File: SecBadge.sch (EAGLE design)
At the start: 21 parts, among them J1 USB_A, U1 32U4, Y1 16MHz

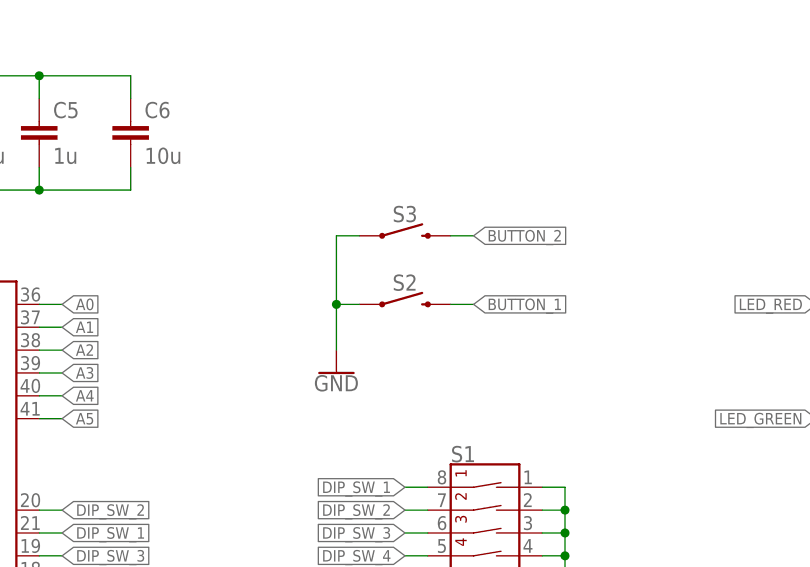
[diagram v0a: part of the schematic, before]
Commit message: Added button designator in schematic.
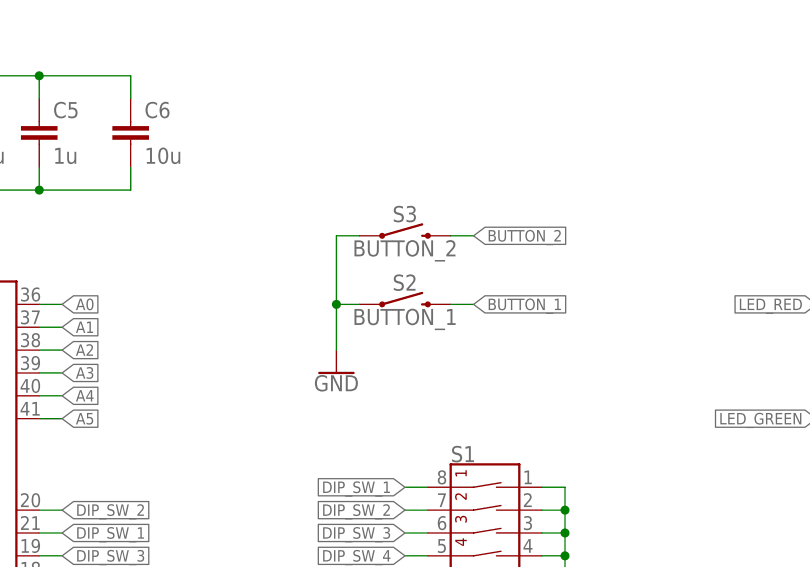
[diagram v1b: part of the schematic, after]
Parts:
- S2: value MOMENTARY-SWITCH-SPST-PTH-6.0MM -> BUTTON_1
- S3: value MOMENTARY-SWITCH-SPST-PTH-6.0MM -> BUTTON_2
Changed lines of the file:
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@@
 <part name="D1" library="ZnibbLib" deviceset="LED" device="" value="RED"/>
 <part name="D2" library="ZnibbLib" deviceset="LED" device="" value="GREEN"/>
-<part name="S2" library="SparkFun-Switches" deviceset="MOMENTARY-SWITCH-SPST" device="-PTH-6.0MM" value=""/>
-<part name="S3" library="SparkFun-Switches" deviceset="MOMENTARY-SWITCH-SPST" device="-PTH-6.0MM" value=""/>
+<part name="S2" library="SparkFun-Switches" deviceset="MOMENTARY-SWITCH-SPST" device="-PTH-6.0MM" value="BUTTON_1"/>
+<part name="S3" library="SparkFun-Switches" deviceset="MOMENTARY-SWITCH-SPST" device="-PTH-6.0MM" value="BUTTON_2"/>
 <part name="R4" library="ZnibbLib" deviceset="RESISTOR" device="1206" value="150"/>
 <part name="R5" library="ZnibbLib" deviceset="RESISTOR" device="1206" value="90"/>

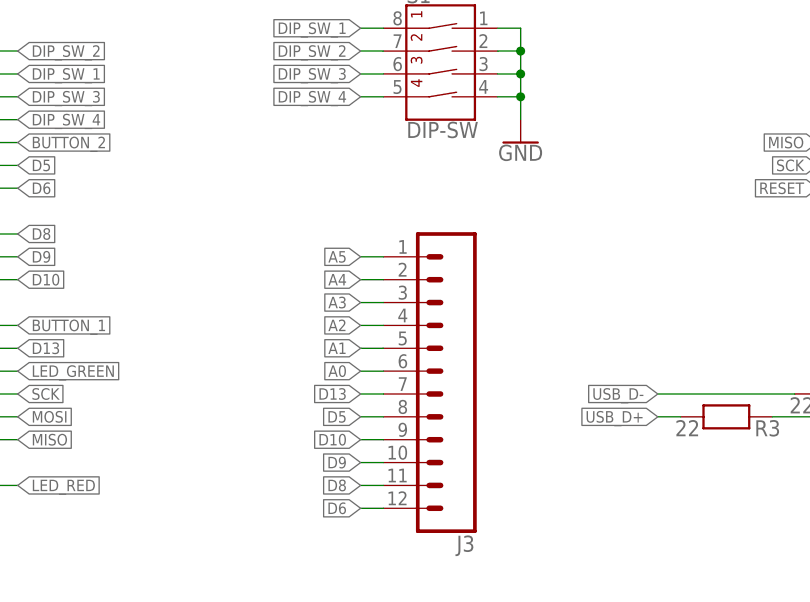
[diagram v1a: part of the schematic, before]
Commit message: Added VCC and GND to expansion header.
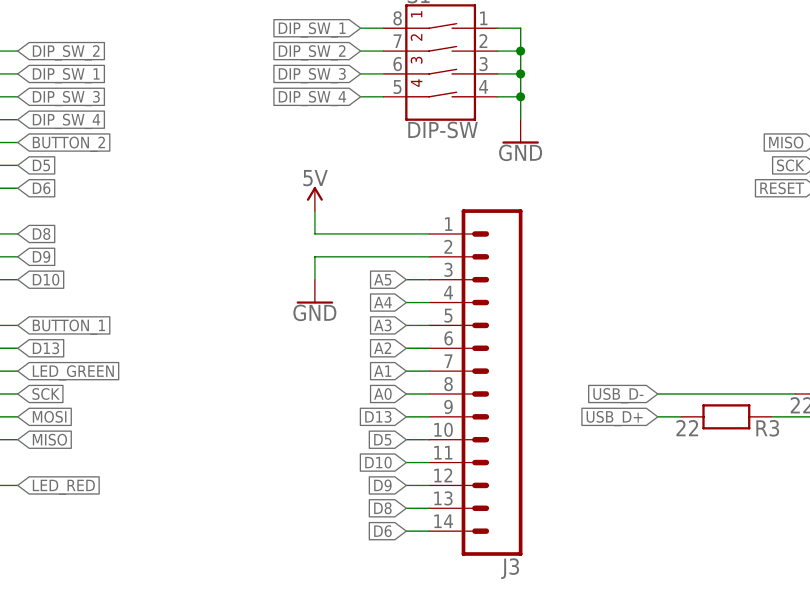
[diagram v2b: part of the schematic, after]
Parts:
- J3: device SparkFun-Connectors:CONN_12 -> SparkFun-Connectors:CONN_14
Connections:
- net 5V: now also J3.1
- net A0: now also J3.8; no longer J3.6
- net A1: now also J3.7; no longer J3.5
- net A2: now also J3.6; no longer J3.4
- net A3: now also J3.5; no longer J3.3
- net A4: now also J3.4; no longer J3.2
- net A5: now also J3.3; no longer J3.1
- net D10: now also J3.11; no longer J3.9
- net D13: now also J3.9; no longer J3.7
- net D5: now also J3.10; no longer J3.8
- net D6: now also J3.14; no longer J3.12
- net D8: now also J3.13; no longer J3.11
- net D9: now also J3.12; no longer J3.10
- net GND: now also J3.2
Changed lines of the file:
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@@
 <part name="GND9" library="PowerSymbols" deviceset="GND" device=""/>
 <part name="J1" library="ZnibbLib" deviceset="USB_A" device=""/>
-<part name="J3" library="SparkFun-Connectors" deviceset="CONN_12" device=""/>
+<part name="J3" library="SparkFun-Connectors" deviceset="CONN_14" device=""/>
+<part name="SUPPLY5" library="PowerSymbols" deviceset="5V" device=""/>
+<part name="GND10" library="PowerSymbols" deviceset="GND" device=""/>
 </parts>
 <sheets>
@@
 <instance part="GND9" gate="1" x="45.72" y="5.08"/>
 <instance part="J1" gate="G$1" x="200.66" y="20.32"/>
-<instance part="J3" gate="G$1" x="137.16" y="22.86" rot="R180"/>
+<instance part="J3" gate="G$1" x="142.24" y="22.86" rot="R180"/>
+<instance part="SUPPLY5" gate="G$1" x="119.38" y="43.18"/>
+<instance part="GND10" gate="1" x="119.38" y="33.02"/>
 </instances>
 <busses>
@@
 <wire x1="198.12" y1="50.8" x2="198.12" y2="53.34" width="0.1524" layer="91"/>
 </segment>
+<segment>
+<pinref part="J3" gate="G$1" pin="1"/>
+<pinref part="SUPPLY5" gate="G$1" pin="5V"/>
+<wire x1="132.08" y1="40.64" x2="119.38" y2="40.64" width="0.1524" layer="91"/>
+<wire x1="119.38" y1="40.64" x2="119.38" y2="43.18" width="0.1524" layer="91"/>
+</segment>
 </net>
 <net name="GND" class="0">
@@
 <junction x="45.72" y="10.16"/>
 </segment>
+<segment>
+<pinref part="J3" gate="G$1" pin="2"/>
+<wire x1="119.38" y1="35.56" x2="119.38" y2="38.1" width="0.1524" layer="91"/>
+<wire x1="119.38" y1="38.1" x2="132.08" y2="38.1" width="0.1524" layer="91"/>
+<pinref part="GND10" gate="1" pin="GND"/>
+</segment>
 </net>
 <net name="N$2" class="0">
@@
 <net name="A5" class="0">
 <segment>
-<pinref part="J3" gate="G$1" pin="1"/>
-<wire x1="124.46" y1="38.1" x2="127" y2="38.1" width="0.1524" layer="91"/>
-<label x="124.46" y="38.1" size="1.27" layer="95" rot="R180" xref="yes"/>
+<wire x1="129.54" y1="35.56" x2="132.08" y2="35.56" width="0.1524" layer="91"/>
+<label x="129.54" y="35.56" size="1.27" layer="95" rot="R180" xref="yes"/>
+<pinref part="J3" gate="G$1" pin="3"/>
 </segment>
 <segment>
@@
 <net name="A4" class="0">
 <segment>
-<pinref part="J3" gate="G$1" pin="2"/>
-<wire x1="124.46" y1="35.56" x2="127" y2="35.56" width="0.1524" layer="91"/>
-<label x="124.46" y="35.56" size="1.27" layer="95" rot="R180" xref="yes"/>
+<wire x1="129.54" y1="33.02" x2="132.08" y2="33.02" width="0.1524" layer="91"/>
+<label x="129.54" y="33.02" size="1.27" layer="95" rot="R180" xref="yes"/>
+<pinref part="J3" gate="G$1" pin="4"/>
 </segment>
 <segment>
@@
 <net name="A3" class="0">
 <segment>
-<pinref part="J3" gate="G$1" pin="3"/>
-<wire x1="124.46" y1="33.02" x2="127" y2="33.02" width="0.1524" layer="91"/>
-<label x="124.46" y="33.02" size="1.27" layer="95" rot="R180" xref="yes"/>
-</segment>
-<segment>
 <pinref part="U1" gate="G$1" pin="PF4(ADC4)"/>
 <wire x1="86.36" y1="76.2" x2="83.82" y2="76.2" width="0.1524" layer="91"/>
 <label x="86.36" y="76.2" size="1.27" layer="95" xref="yes"/>
 </segment>
+<segment>
+<pinref part="J3" gate="G$1" pin="5"/>
+<wire x1="129.54" y1="30.48" x2="132.08" y2="30.48" width="0.1524" layer="91"/>
+<label x="129.54" y="30.48" size="1.27" layer="95" rot="R180" xref="yes"/>
+</segment>
 </net>
 <net name="A2" class="0">
 <segment>
-<pinref part="J3" gate="G$1" pin="4"/>
-<wire x1="124.46" y1="30.48" x2="127" y2="30.48" width="0.1524" layer="91"/>
-<label x="124.46" y="30.48" size="1.27" layer="95" rot="R180" xref="yes"/>
+<wire x1="129.54" y1="27.94" x2="132.08" y2="27.94" width="0.1524" layer="91"/>
+<label x="129.54" y="27.94" size="1.27" layer="95" rot="R180" xref="yes"/>
+<pinref part="J3" gate="G$1" pin="6"/>
 </segment>
 <segment>
@@
 <net name="A1" class="0">
 <segment>
-<pinref part="J3" gate="G$1" pin="5"/>
-<wire x1="124.46" y1="27.94" x2="127" y2="27.94" width="0.1524" layer="91"/>
-<label x="124.46" y="27.94" size="1.27" layer="95" rot="R180" xref="yes"/>
+<wire x1="129.54" y1="25.4" x2="132.08" y2="25.4" width="0.1524" layer="91"/>
+<label x="129.54" y="25.4" size="1.27" layer="95" rot="R180" xref="yes"/>
+<pinref part="J3" gate="G$1" pin="7"/>
 </segment>
 <segment>
@@
 <net name="A0" class="0">
 <segment>
-<pinref part="J3" gate="G$1" pin="6"/>
-<wire x1="124.46" y1="25.4" x2="127" y2="25.4" width="0.1524" layer="91"/>
-<label x="124.46" y="25.4" size="1.27" layer="95" rot="R180" xref="yes"/>
+<wire x1="129.54" y1="22.86" x2="132.08" y2="22.86" width="0.1524" layer="91"/>
+<label x="129.54" y="22.86" size="1.27" layer="95" rot="R180" xref="yes"/>
+<pinref part="J3" gate="G$1" pin="8"/>
 </segment>
 <segment>
@@
 <net name="D13" class="0">
 <segment>
-<pinref part="J3" gate="G$1" pin="7"/>
-<wire x1="124.46" y1="22.86" x2="127" y2="22.86" width="0.1524" layer="91"/>
-<label x="124.46" y="22.86" size="1.27" layer="95" rot="R180" xref="yes"/>
+<wire x1="129.54" y1="20.32" x2="132.08" y2="20.32" width="0.1524" layer="91"/>
+<label x="129.54" y="20.32" size="1.27" layer="95" rot="R180" xref="yes"/>
+<pinref part="J3" gate="G$1" pin="9"/>
 </segment>
 <segment>
@@
 <net name="D5" class="0">
 <segment>
-<pinref part="J3" gate="G$1" pin="8"/>
-<wire x1="124.46" y1="20.32" x2="127" y2="20.32" width="0.1524" layer="91"/>
-<label x="124.46" y="20.32" size="1.27" layer="95" rot="R180" xref="yes"/>
+<wire x1="129.54" y1="17.78" x2="132.08" y2="17.78" width="0.1524" layer="91"/>
+<label x="129.54" y="17.78" size="1.27" layer="95" rot="R180" xref="yes"/>
+<pinref part="J3" gate="G$1" pin="10"/>
 </segment>
 <segment>
@@
 <net name="D10" class="0">
 <segment>
-<pinref part="J3" gate="G$1" pin="9"/>
-<wire x1="124.46" y1="17.78" x2="127" y2="17.78" width="0.1524" layer="91"/>
-<label x="124.46" y="17.78" size="1.27" layer="95" rot="R180" xref="yes"/>
+<wire x1="129.54" y1="15.24" x2="132.08" y2="15.24" width="0.1524" layer="91"/>
+<label x="129.54" y="15.24" size="1.27" layer="95" rot="R180" xref="yes"/>
+<pinref part="J3" gate="G$1" pin="11"/>
 </segment>
 <segment>
@@
 <net name="D9" class="0">
 <segment>
-<pinref part="J3" gate="G$1" pin="10"/>
-<wire x1="124.46" y1="15.24" x2="127" y2="15.24" width="0.1524" layer="91"/>
-<label x="124.46" y="15.24" size="1.27" layer="95" rot="R180" xref="yes"/>
+<wire x1="129.54" y1="12.7" x2="132.08" y2="12.7" width="0.1524" layer="91"/>
+<label x="129.54" y="12.7" size="1.27" layer="95" rot="R180" xref="yes"/>
+<pinref part="J3" gate="G$1" pin="12"/>
 </segment>
 <segment>
@@
 <net name="D8" class="0">
 <segment>
-<pinref part="J3" gate="G$1" pin="11"/>
-<wire x1="124.46" y1="12.7" x2="127" y2="12.7" width="0.1524" layer="91"/>
-<label x="124.46" y="12.7" size="1.27" layer="95" rot="R180" xref="yes"/>
+<wire x1="129.54" y1="10.16" x2="132.08" y2="10.16" width="0.1524" layer="91"/>
+<label x="129.54" y="10.16" size="1.27" layer="95" rot="R180" xref="yes"/>
+<pinref part="J3" gate="G$1" pin="13"/>
 </segment>
 <segment>
@@
 <net name="D6" class="0">
 <segment>
-<pinref part="J3" gate="G$1" pin="12"/>
-<wire x1="124.46" y1="10.16" x2="127" y2="10.16" width="0.1524" layer="91"/>
-<label x="124.46" y="10.16" size="1.27" layer="95" rot="R180" xref="yes"/>
-</segment>
-<segment>
+<wire x1="129.54" y1="7.62" x2="132.08" y2="7.62" width="0.1524" layer="91"/>
+<label x="129.54" y="7.62" size="1.27" layer="95" rot="R180" xref="yes"/>
+<pinref part="J3" gate="G$1" pin="14"/>
+</segment>
+<segment>
